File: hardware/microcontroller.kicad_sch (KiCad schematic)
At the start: 19 parts, among them J2 STLink Header, SW1 BOOT, SW2 RESET, SW3 USER0, SW4 USER2, SW5 USER1, SW6 USER3, U1 STM32G474QBT6

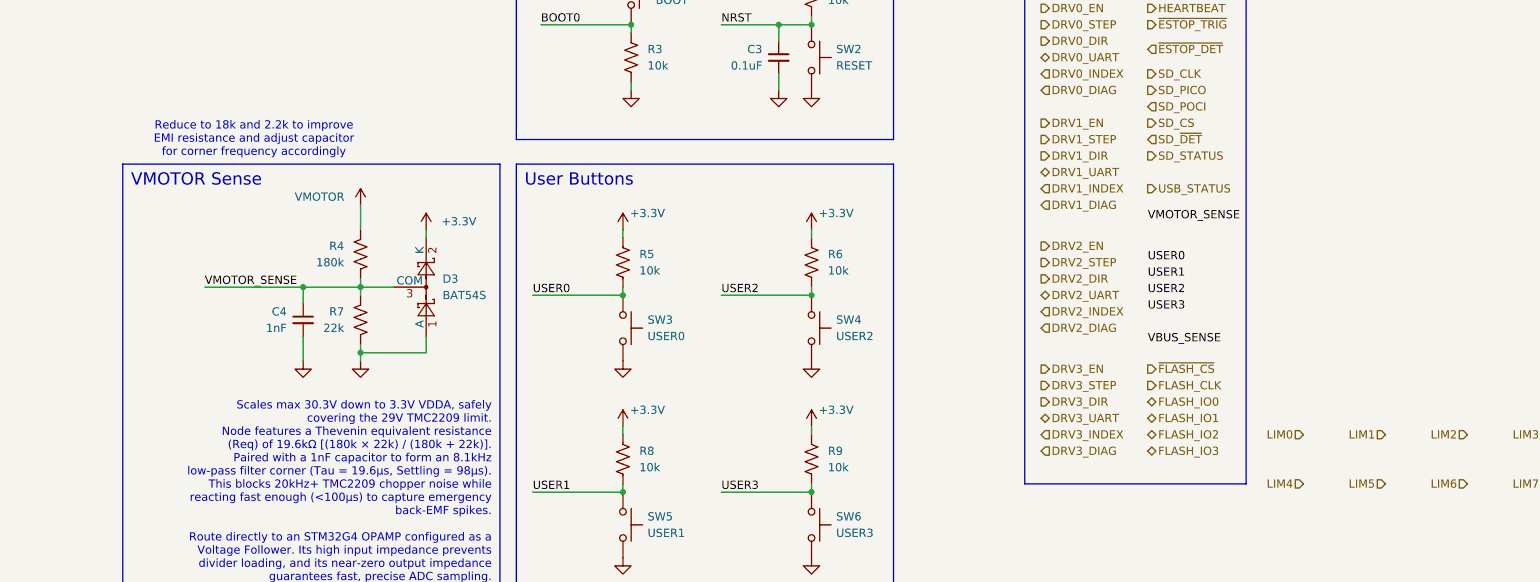
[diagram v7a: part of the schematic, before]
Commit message: Add EEPROM
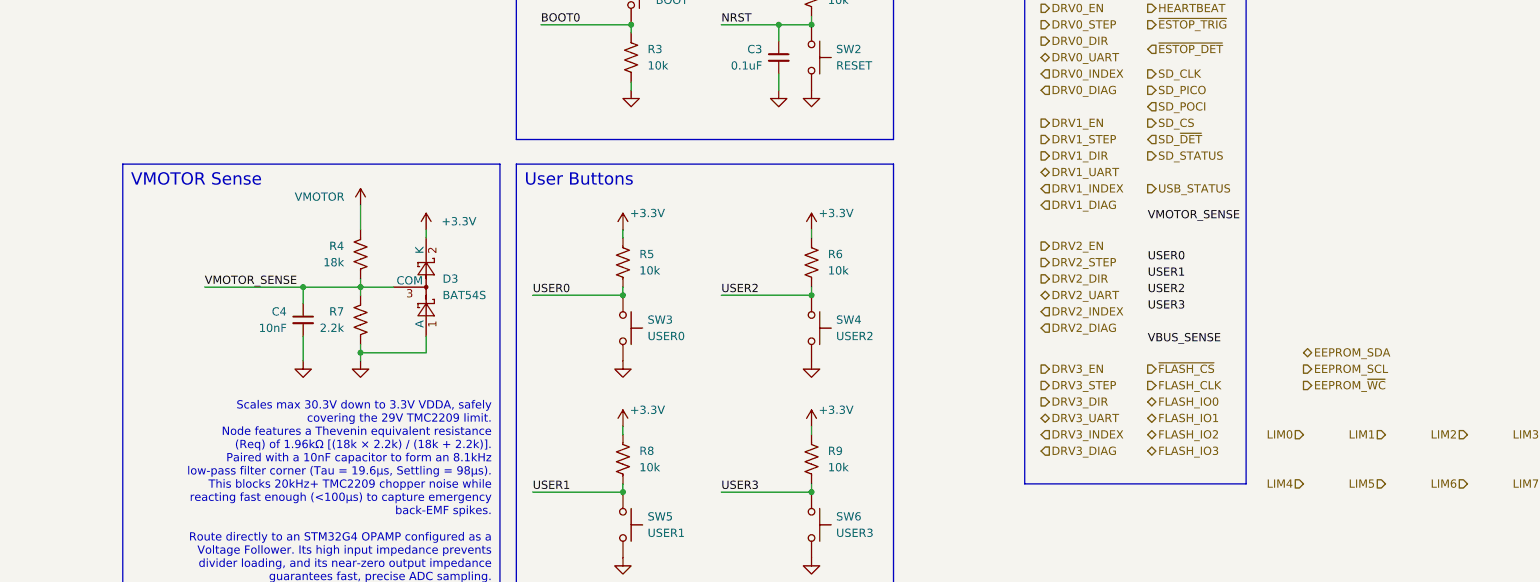
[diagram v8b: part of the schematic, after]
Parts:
- C4: value 1nF -> 10nF; Part Number C0603C102K5RACTU -> GCM155R71H103KA55D; Vendor URL https://www.digikey.com/en/products/detail/kemet/C0603C102K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 -> https://www.digikey.com/en/products/detail/murata-electroni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
- R4: value 180k -> 18k; Part Number (none) -> RC0603FR-0718KL; Vendor URL (none) -> https://www.digikey.com/en/products/detail/yageo/RC0603FR-0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
- R7: value 22k -> 2.2k; Part Number (none) -> RC0603FR-072K2L; Vendor URL (none) -> https://www.digikey.com/en/products/detail/yageo/RC0603FR-0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
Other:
- note added: "Scales max 30.3V down to 3.3V VDDA, safely covering the 29V TMC2209 limit. Node features a Thevenin equivalent resistance (Req) of 1.96kΩ [(18k × 2.2k) / (18k + 2.2k)]. Paired with a 10nF capacitor to form an 8.1kHz low-pass filter corner (Tau = 19.6µs, Settling = 98µs). This blocks 20kHz+ TMC2209 chopper noise while reacting fast enough (<100µs) to capture emergency back-EMF spikes. Route direct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"
- note removed: "Reduce to 18k and 2.2k to improve EMI resistance and adjust capacitor for corner frequency accordingly"
- note removed: "Scales max 30.3V down to 3.3V VDDA, safely covering the 29V TMC2209 limit. Node features a Thevenin equivalent resistance (Req) of 19.6kΩ [(180k × 22k) / (180k + 22k)]. Paired with a 1nF capacitor to form an 8.1kHz low-pass filter corner (Tau = 19.6µs, Settling = 98µs). This blocks 20kHz+ TMC2209 chopper noise while reacting fast enough (<100µs) to capture emergency back-EMF spikes. Route directl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"
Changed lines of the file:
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@@
 		)
 	)
-	(text "Reduce to 18k and 2.2k to improve\nEMI resistance and adjust capacitor\nfor corner frequency accordingly"
-		(exclude_from_sim no)
-		(at 165.1 99.06 0)
-		(effects
-			(font
-				(size 1.27 1.27)
-				(color 132 0 0 1)
-			)
-		)
-	)
 	(text "VMOTOR Sense"
 		(exclude_from_sim no)
@@
 		)
 	)
-	(text "Scales max 30.3V down to 3.3V VDDA, safely\ncovering the 29V TMC2209 limit.\nNode features a Thevenin equivalent resistance\n(Req) of 19.6kΩ [(180k × 22k) / (180k + 22k)].\nPaired with a 1nF capacitor to form an 8.1kHz\nlow-pass filter corner (Tau = 19.6µs, Settling = 98µs).\nThis blocks 20kHz+ TMC2209 chopper noise while \nreacting fast enough (<100µs) to capture emergency\nback-EMF spikes.\n\nRoute directly to an STM32G4 OPAMP configured as a \n Voltage Follower. Its high input impedance prevents\ndivider loading, and its near-zero output impedance\nguarantees fast, precise ADC sampling."
+	(text "Scales max 30.3V down to 3.3V VDDA, safely\ncovering the 29V TMC2209 limit.\nNode features a Thevenin equivalent resistance\n(Req) of 1.96kΩ [(18k × 2.2k) / (18k + 2.2k)].\nPaired with a 10nF capacitor to form an 8.1kHz\nlow-pass filter corner (Tau = 19.6µs, Settling = 98µs).\nThis blocks 20kHz+ TMC2209 chopper noise while \nreacting fast enough (<100µs) to capture emergency\nback-EMF spikes.\n\nRoute directly to an STM32G4 OPAMP configured as a \n Voltage Follower. Its high input impedance prevents\ndivider loading, and its near-zero output impedance\nguarantees fast, precise ADC sampling."
 		(exclude_from_sim no)
 		(at 201.93 153.67 0)
@@
 		)
 	)
+	(hierarchical_label "EEPROM_SDA"
+		(shape bidirectional)
+		(at 327.66 132.08 0)
+		(effects
+			(font
+				(size 1.27 1.27)
+				(thickness 0.1588)
+			)
+			(justify left)
+		)
+	)
 	(hierarchical_label "DRV2_INDEX"
 		(shape input)
@@
 		)
 	)
+	(hierarchical_label "EEPROM_~{WC}"
+		(shape output)
+		(at 327.66 137.16 0)
+		(effects
+			(font
+				(size 1.27 1.27)
+				(thickness 0.1588)
+			)
+			(justify left)
+		)
+	)
 	(hierarchical_label "LIM7"
 		(shape input)
@@
 		)
 	)
+	(hierarchical_label "EEPROM_SCL"
+		(shape output)
+		(at 327.66 134.62 0)
+		(effects
+			(font
+				(size 1.27 1.27)
+				(thickness 0.1588)
+			)
+			(justify left)
+		)
+	)
 	(hierarchical_label "USB_STATUS"
 		(shape output)
@@
 			)
 		)
-		(property "Value" "1nF"
+		(property "Value" "10nF"
 			(at 170.18 128.2762 0)
 			(show_name no)
@@
 			)
 		)
-		(property "Part Number" "C0603C102K5RACTU"
+		(property "Part Number" "GCM155R71H103KA55D"
 			(at 172.72 127 0)
 			(hide yes)
@@
 			)
 		)
-		(property "Vendor URL" "https://www.digikey.com/en/products/detail/kemet/C0603C102K5RACTU/411081"
+		(property "Vendor URL" "https://www.digikey.com/en/products/detail/murata-electronics/GCM155R71H103KA55D/1641636"
 			(at 172.72 127 0)
 			(hide yes)
@@
 			)
 		)
-		(property "Value" "180k"
+		(property "Value" "18k"
 			(at 179.07 118.1099 0)
 			(show_name no)
@@
 			)
 		)
+		(property "Part Number" "RC0603FR-0718KL"
+			(at 181.61 116.84 0)
+			(hide yes)
+			(show_name no)
+			(do_not_autoplace no)
+			(effects
+				(font
+					(size 1.27 1.27)
+				)
+			)
+		)
+		(property "Vendor URL" "https://www.digikey.com/en/products/detail/yageo/RC0603FR-0718KL/726989"
+			(at 181.61 116.84 0)
+			(hide yes)
+			(show_name no)
+			(do_not_autoplace no)
+			(effects
+				(font
+					(size 1.27 1.27)
+				)
+			)
+		)
 		(pin "1"
 		)
@@
 			)
 		)
-		(property "Value" "22k"
+		(property "Value" "2.2k"
 			(at 179.07 128.2699 0)
 			(show_name no)
@@
 			(at 181.61 127 0)
 			(hide yes)
+			(show_name no)
+			(do_not_autoplace no)
+			(effects
+				(font
+					(size 1.27 1.27)
+				)
+			)
+		)
+		(property "Part Number" "RC0603FR-072K2L"
+			(at 181.61 127 0)
+			(hide yes)
+			(show_name no)
+			(do_not_autoplace no)
+			(effects
+				(font
+					(size 1.27 1.27)
+				)
+			)
+		)
+		(property "Vendor URL" "https://www.digikey.com/en/products/detail/yageo/RC0603FR-072K2L/727016"
+			(at 181.61 127 0)
+			(hide yes)
